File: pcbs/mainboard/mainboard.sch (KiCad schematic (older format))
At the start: 30 parts, among them J1 USB_B_Micro, SW1 SW_MEC_5E, SW2 SW_MEC_5E, U1 ATmega32U4-AU, U2 USBLC6-2SC6, U3 XC6206P332MR, U4 XC9572XL-10VQG44C, Y1 16MHz

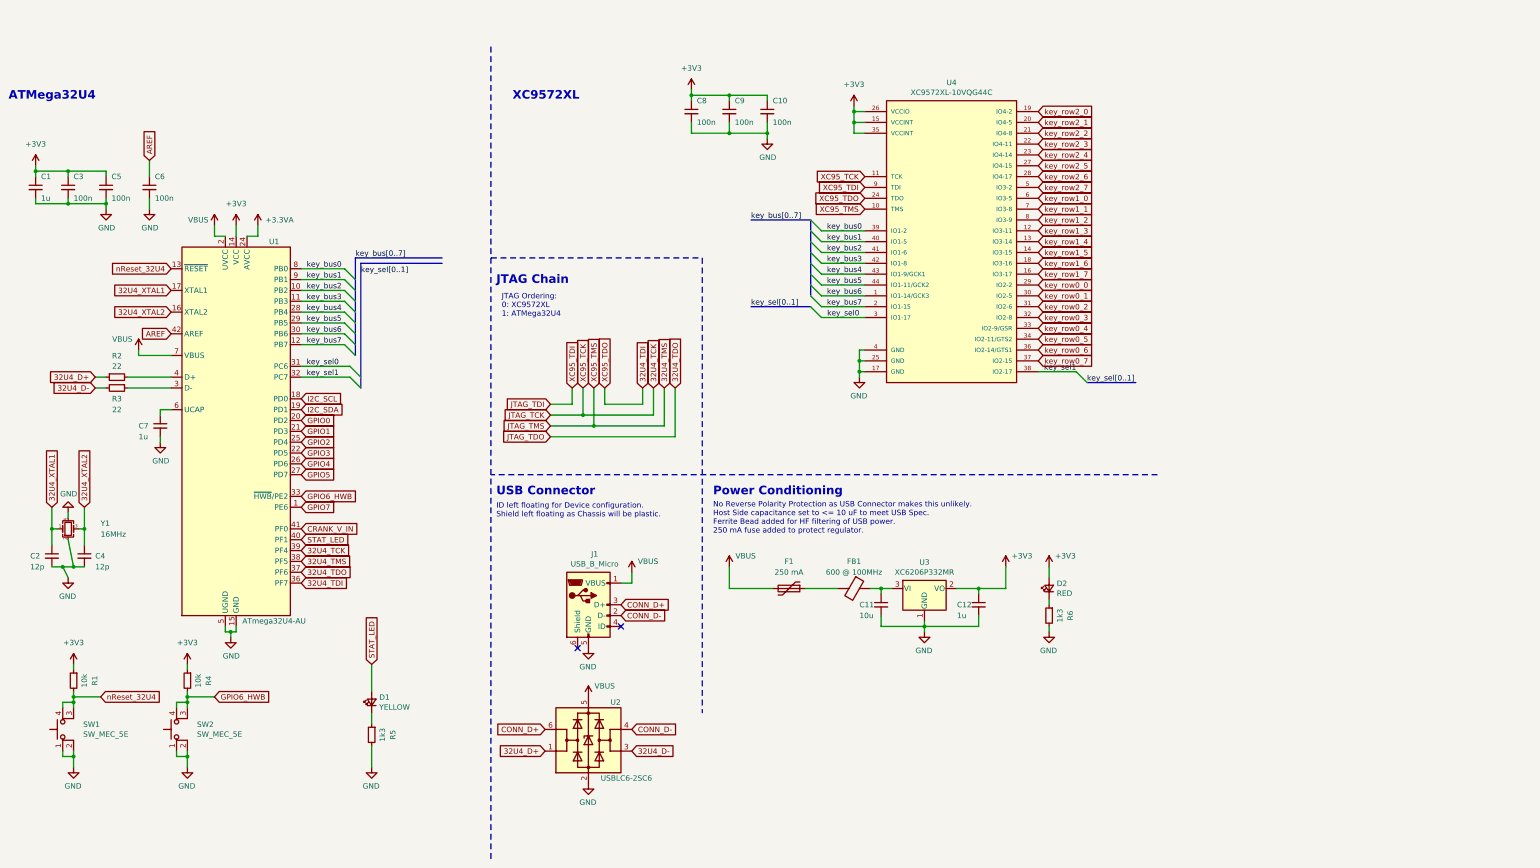
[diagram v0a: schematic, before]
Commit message: Add completed schematic with footprints
Add completed schematic with connectors for all IO and programming
devices.

Connectors laid out on a separate sheet.

DRC check completed.
One rule left unfulfilled resulting from KiCAD not recognising when
a power signal has run all but undisturbed through a power filter.
This affects the VBUS flag.
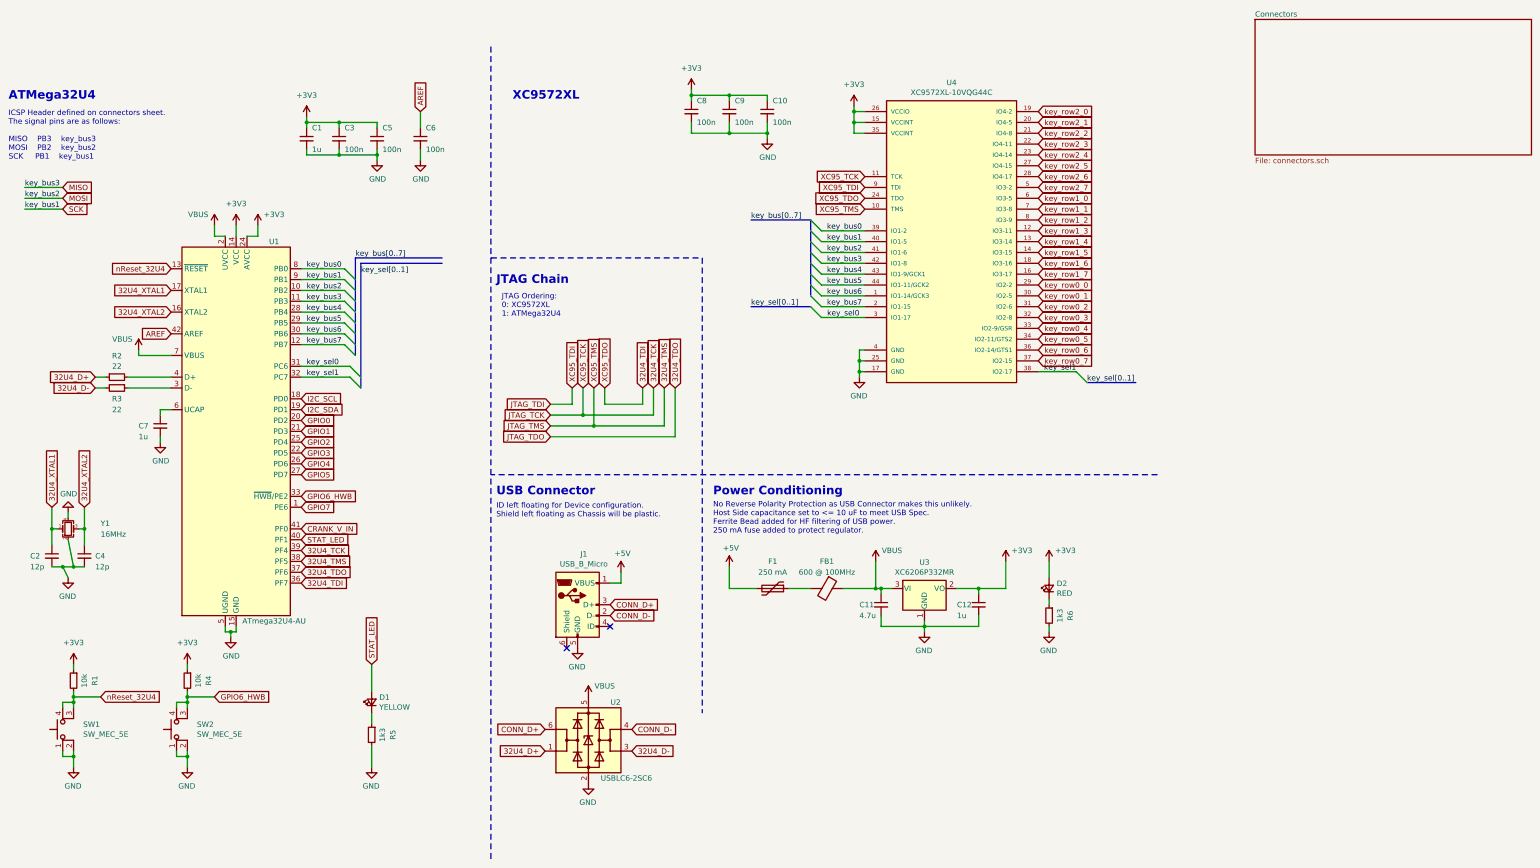
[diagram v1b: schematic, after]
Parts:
- C1, C10, C12, C2, C3, C4, C5, C6, C7, C8, C9: footprint (none) -> Capacitor_SMD:C_0603_1608Metric
- C11: value 10u -> 4.7u; footprint (none) -> Capacitor_SMD:C_0603_1608Metric
- F1: footprint (none) -> Fuse:Fuse_1206_3216Metric
- FB1: footprint (none) -> Inductor_SMD:L_0805_2012Metric
- R1, R2, R3, R4, R5, R6: footprint (none) -> Resistor_SMD:R_0603_1608Metric
- Y1: footprint (none) -> Crystal:Crystal_SMD_3225-4Pin_3.2x2.5mm
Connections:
- net +3.3VA is gone; now on net +3V3: U1.24 (AVCC), U1.44 (AVCC)
- net VBUS: now also C11.1, FB1.1, U3.3 (VI); no longer F1.2, J1.1 (VBUS)
- net key_bus1 renamed SCK
- net key_bus2 renamed MOSI
- net key_bus3 renamed MISO
- new net +5V: F1.2, J1.1 (VBUS)
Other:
- note added: "ICSP Header defined on connectors sheet.\nThe signal pins are as follows:\n\nMISO PB3 key_bus3\nMOSI PB2 key_bus2\nSCK PB1 key_bus1"
- moved on the sheet: C1, C3, C5, C6, F1, FB1, J1

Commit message: Add 3V3A filter and JLC Part numbers
Add a single stage LC filter to the ADC power input.
Design taken from Fig. 24-10 in 32U4 datasheet.

Add JLC part numbers for all SMD parts.
XC95 part was out of stock at time of commit.
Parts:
- added C13: 100n, Capacitor_SMD:C_0603_1608Metric, symbol Device:C_Small
- added L1: 10u, Inductor_SMD:L_1206_3216Metric, symbol Device:L_Small
- C1, C12, C7: JLCPCB Part # (none) -> 0603
- C10, C3, C5, C6, C8, C9: JLCPCB Part # (none) -> C14663
- C11: JLCPCB Part # (none) -> C19666
- C2, C4: JLCPCB Part # (none) -> C38523
- D1: JLCPCB Part # (none) -> C72038
- D2: JLCPCB Part # (none) -> C2286
- R1, R4: JLCPCB Part # (none) -> C25804
- R2, R3: JLCPCB Part # (none) -> C23345
- R5, R6: value 1k3 -> 1k; JLCPCB Part # (none) -> C21190
- U1: JLCPCB Part # (none) -> C44854
- U4: JLCPCB Part # (none) -> C569042
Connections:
- net +3V3: now also L1.1; no longer U1.24 (AVCC), U1.44 (AVCC)
- net GND: now also C13.2
- new net +3.3VA: C13.1, L1.2, U1.24 (AVCC), U1.44 (AVCC)
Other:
- note added: "ICSP Header defined on connectors sheet.\nThe signal pins are as follows:\n\nMISO PB3 key_bus3\nMOSI PB2 key_bus2\nSCK PB1 key_bus1\n\nLC filter for +3V3A analog power bus taken \nfrom Fig. 24-10 in 32U4 datasheet."
- note removed: "ICSP Header defined on connectors sheet.\nThe signal pins are as follows:\n\nMISO PB3 key_bus3\nMOSI PB2 key_bus2\nSCK PB1 key_bus1"
- moved on the sheet: C1, C3, C5, C6

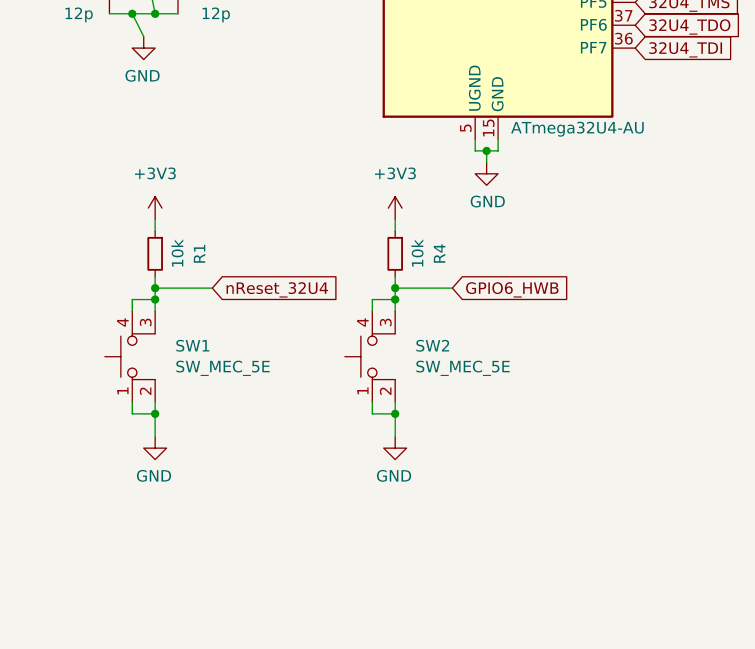
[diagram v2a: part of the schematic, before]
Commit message: Add mounting holes and fix button footprint
Replace button footprint with one which matches the symbol.
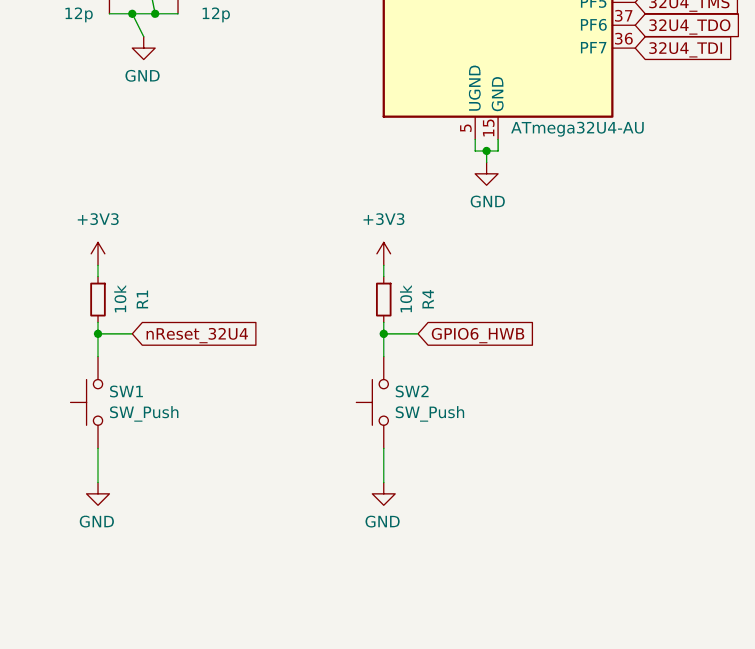
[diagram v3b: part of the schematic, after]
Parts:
- removed SW1, SW2: SW_MEC_5E, Button_Switch_THT:SW_PUSH_6mm, symbol Switch:SW_MEC_5E
- added SW1, SW2: SW_Push, Button_Switch_THT:SW_PUSH_6mm, symbol Switch:SW_Push
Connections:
- net GND: now also SW1.1, SW2.1
- net GPIO6_HWB: now also SW2.2
- net nReset_32U4: now also SW1.2
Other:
- moved on the sheet: R1, R4
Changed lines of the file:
@@
 L Device:R_Small R1
 U 1 1 613EE75F
-P 1300 6250
-F 0 "R1" V 1104 6250 50  0000 C CNN
-F 1 "10k" V 1200 6250 50  0000 C CNN
-F 2 "Resistor_SMD:R_0603_1608Metric" H 1300 6250 50  0001 C CNN
-F 3 "~" H 1300 6250 50  0001 C CNN
-F 4 "C25804" H 1300 6250 50  0001 C CNN "JLCPCB Part #"
-	1    1300 6250
-	-1   0    0    -1
-$EndComp
-Wire Wire Line
-	1300 6350 1300 6400
+P 1050 6450
+F 0 "R1" V 854 6450 50  0000 C CNN
+F 1 "10k" V 950 6450 50  0000 C CNN
+F 2 "Resistor_SMD:R_0603_1608Metric" H 1050 6450 50  0001 C CNN
+F 3 "~" H 1050 6450 50  0001 C CNN
+F 4 "C25804" H 1050 6450 50  0001 C CNN "JLCPCB Part #"
+	1    1050 6450
+	-1   0    0    -1
+$EndComp
+Wire Wire Line
+	1050 6550 1050 6600
 $Comp
 L power:GND #PWR05
 U 1 1 613EFD99
-P 1300 7050
-F 0 "#PWR05" H 1300 6800 50  0001 C CNN
-F 1 "GND" H 1305 6877 50  0000 C CNN
-F 2 "" H 1300 7050 50  0001 C CNN
-F 3 "" H 1300 7050 50  0001 C CNN
-	1    1300 7050
-	-1   0    0    -1
-$EndComp
-$Comp
-L Switch:SW_MEC_5E SW1
-U 1 1 613DF71C
-P 1300 6700
-F 0 "SW1" V 1346 6612 50  0000 R CNN
-F 1 "SW_MEC_5E" V 1255 6612 50  0000 R CNN
-F 2 "Button_Switch_THT:SW_PUSH_6mm" H 1300 7000 50  0001 C CNN
-F 3 "http://www.apem.com/int/index.php?controller=attachment&id_attachment=1371" H 1300 7000 50  0001 C CNN
-	1    1300 6700
-	0    -1   -1   0
-$EndComp
-Wire Wire Line
-	1200 6500 1200 6450
-Wire Wire Line
-	1200 6450 1300 6450
-Connection ~ 1300 6450
-Wire Wire Line
-	1300 6450 1300 6500
-Wire Wire Line
-	1300 6400 1550 6400
-Connection ~ 1300 6400
-Wire Wire Line
-	1300 6400 1300 6450
-Text GLabel 1550 6400 2    50   Input ~ 0
+P 1050 7250
+F 0 "#PWR05" H 1050 7000 50  0001 C CNN
+F 1 "GND" H 1055 7077 50  0000 C CNN
+F 2 "" H 1050 7250 50  0001 C CNN
+F 3 "" H 1050 7250 50  0001 C CNN
+	1    1050 7250
+	-1   0    0    -1
+$EndComp
+Wire Wire Line
+	1050 6600 1200 6600
+Connection ~ 1050 6600
+Text GLabel 1200 6600 2    50   Input ~ 0
 nReset_32U4
 $Comp
 L power:+3V3 #PWR04
 U 1 1 613F7F25
-P 1300 6100
-F 0 "#PWR04" H 1300 5950 50  0001 C CNN
-F 1 "+3V3" H 1300 6300 50  0000 C CNN
-F 2 "" H 1300 6100 50  0001 C CNN
-F 3 "" H 1300 6100 50  0001 C CNN
-	1    1300 6100
-	-1   0    0    -1
-$EndComp
-Wire Wire Line
-	1300 6100 1300 6150
-Wire Wire Line
-	1300 6900 1300 6950
-Wire Wire Line
-	1300 6950 1200 6950
-Wire Wire Line
-	1200 6950 1200 6900
-Connection ~ 1300 6950
-Wire Wire Line
-	1300 6950 1300 7050
+P 1050 6300
+F 0 "#PWR04" H 1050 6150 50  0001 C CNN
+F 1 "+3V3" H 1050 6500 50  0000 C CNN
+F 2 "" H 1050 6300 50  0001 C CNN
+F 3 "" H 1050 6300 50  0001 C CNN
+	1    1050 6300
+	-1   0    0    -1
+$EndComp
+Wire Wire Line
+	1050 6300 1050 6350
 Wire Wire Line
 	3400 2450 3800 2450
@@
 L Device:R_Small R4
 U 1 1 61478CC9
-P 2350 6250
-F 0 "R4" V 2154 6250 50  0000 C CNN
-F 1 "10k" V 2250 6250 50  0000 C CNN
-F 2 "Resistor_SMD:R_0603_1608Metric" H 2350 6250 50  0001 C CNN
-F 3 "~" H 2350 6250 50  0001 C CNN
-F 4 "C25804" H 2350 6250 50  0001 C CNN "JLCPCB Part #"
-	1    2350 6250
-	-1   0    0    -1
-$EndComp
-Wire Wire Line
-	2350 6350 2350 6400
+P 2300 6450
+F 0 "R4" V 2104 6450 50  0000 C CNN
+F 1 "10k" V 2200 6450 50  0000 C CNN
+F 2 "Resistor_SMD:R_0603_1608Metric" H 2300 6450 50  0001 C CNN
+F 3 "~" H 2300 6450 50  0001 C CNN
+F 4 "C25804" H 2300 6450 50  0001 C CNN "JLCPCB Part #"
+	1    2300 6450
+	-1   0    0    -1
+$EndComp
+Wire Wire Line
+	2300 6550 2300 6600
 $Comp
 L power:GND #PWR011
 U 1 1 61478CD4
-P 2350 7050
-F 0 "#PWR011" H 2350 6800 50  0001 C CNN
-F 1 "GND" H 2355 6877 50  0000 C CNN
-F 2 "" H 2350 7050 50  0001 C CNN
-F 3 "" H 2350 7050 50  0001 C CNN
-	1    2350 7050
-	-1   0    0    -1
-$EndComp
-$Comp
-L Switch:SW_MEC_5E SW2
-U 1 1 61478CDE
-P 2350 6700
-F 0 "SW2" V 2396 6612 50  0000 R CNN
-F 1 "SW_MEC_5E" V 2305 6612 50  0000 R CNN
-F 2 "Button_Switch_THT:SW_PUSH_6mm" H 2350 7000 50  0001 C CNN
-F 3 "http://www.apem.com/int/index.php?controller=attachment&id_attachment=1371" H 2350 7000 50  0001 C CNN
-	1    2350 6700
-	0    -1   -1   0
-$EndComp
-Wire Wire Line
-	2250 6500 2250 6450
-Wire Wire Line
-	2250 6450 2350 6450
-Connection ~ 2350 6450
-Wire Wire Line
-	2350 6450 2350 6500
-Wire Wire Line
-	2350 6400 2600 6400
-Connection ~ 2350 6400
-Wire Wire Line
-	2350 6400 2350 6450
+P 2300 7250
+F 0 "#PWR011" H 2300 7000 50  0001 C CNN
+F 1 "GND" H 2305 7077 50  0000 C CNN
+F 2 "" H 2300 7250 50  0001 C CNN
+F 3 "" H 2300 7250 50  0001 C CNN
+	1    2300 7250
+	-1   0    0    -1
+$EndComp
+Wire Wire Line
+	2300 6600 2450 6600
+Connection ~ 2300 6600
 $Comp
 L power:+3V3 #PWR010
 U 1 1 61478CF0
-P 2350 6100
-F 0 "#PWR010" H 2350 5950 50  0001 C CNN
-F 1 "+3V3" H 2350 6300 50  0000 C CNN
-F 2 "" H 2350 6100 50  0001 C CNN
-F 3 "" H 2350 6100 50  0001 C CNN
-	1    2350 6100
-	-1   0    0    -1
-$EndComp
-Wire Wire Line
-	2350 6100 2350 6150
-Wire Wire Line
-	2350 6900 2350 6950
-Wire Wire Line
-	2350 6950 2250 6950
-Wire Wire Line
-	2250 6950 2250 6900
-Connection ~ 2350 6950
-Wire Wire Line
-	2350 6950 2350 7050
-Text GLabel 2600 6400 2    50   Input ~ 0
+P 2300 6300
+F 0 "#PWR010" H 2300 6150 50  0001 C CNN
+F 1 "+3V3" H 2300 6500 50  0000 C CNN
+F 2 "" H 2300 6300 50  0001 C CNN
+F 3 "" H 2300 6300 50  0001 C CNN
+	1    2300 6300
+	-1   0    0    -1
+$EndComp
+Wire Wire Line
+	2300 6300 2300 6350
+Text GLabel 2450 6600 2    50   Input ~ 0
 GPIO6_HWB
 Wire Wire Line
@@
 Wire Bus Line
 	3900 2350 3900 3250
+Wire Wire Line
+	2300 6600 2300 6700
+Wire Wire Line
+	2300 7100 2300 7250
+Wire Wire Line
+	1050 6600 1050 6700
+Wire Wire Line
+	1050 7100 1050 7250
+$Comp
+L Switch:SW_Push SW1
+U 1 1 615F31C2
+P 1050 6900
+F 0 "SW1" V 1096 6852 50  0000 R CNN
+F 1 "SW_Push" V 1005 6852 50  0000 R CNN
+F 2 "Button_Switch_THT:SW_PUSH_6mm" H 1050 7100 50  0001 C CNN
+F 3 "~" H 1050 7100 50  0001 C CNN
+	1    1050 6900
+	0    -1   -1   0
+$EndComp
+$Comp
+L Switch:SW_Push SW2
+U 1 1 615F39C9
+P 2300 6900
+F 0 "SW2" V 2346 6852 50  0000 R CNN
+F 1 "SW_Push" V 2255 6852 50  0000 R CNN
+F 2 "Button_Switch_THT:SW_PUSH_6mm" H 2300 7100 50  0001 C CNN
+F 3 "~" H 2300 7100 50  0001 C CNN
+	1    2300 6900
+	0    -1   -1   0
+$EndComp
 $EndSCHEMATC
